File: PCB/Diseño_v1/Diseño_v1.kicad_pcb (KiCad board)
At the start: 2 copper layers, 100 x 100 mm, 7 parts

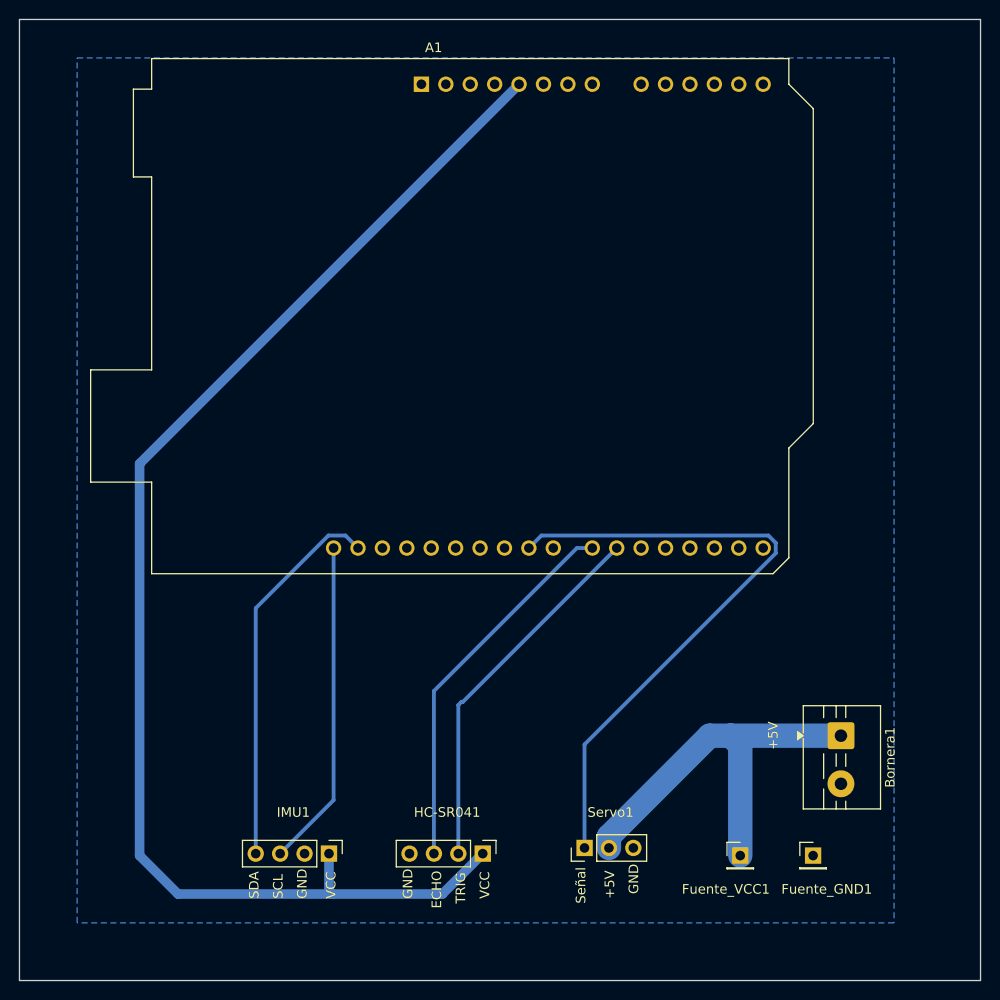
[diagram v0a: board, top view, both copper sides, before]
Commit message: Modifiqué el PCB
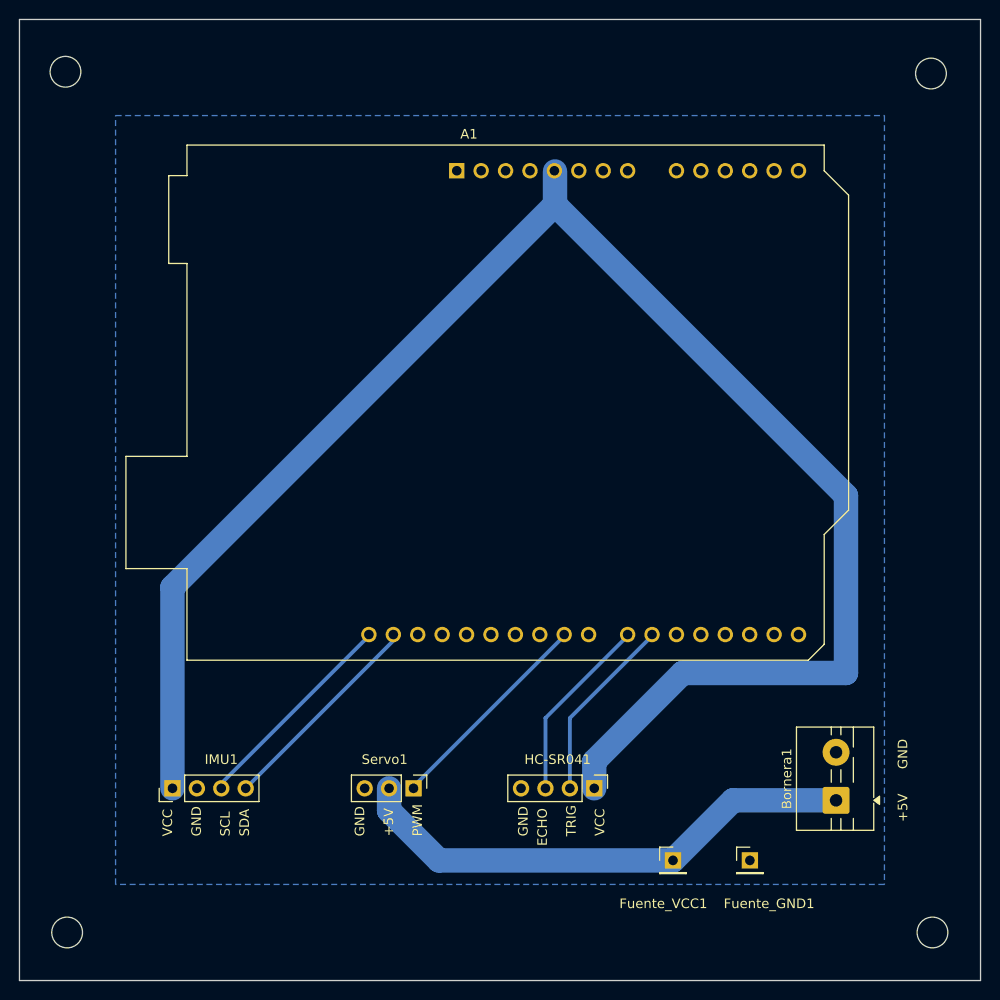
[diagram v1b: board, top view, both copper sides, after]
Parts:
- added REF**: MountingHole_3.2mm_M3, MountingHole:MountingHole_3.2mm_M3, F.Cu at (105.0, 145.0)
- added REF**: MountingHole_3.2mm_M3, MountingHole:MountingHole_3.2mm_M3, F.Cu at (195.0, 145.0)
- added REF**: MountingHole_3.2mm_M3, MountingHole:MountingHole_3.2mm_M3, F.Cu at (104.8, 55.4)
- added REF**: MountingHole_3.2mm_M3, MountingHole:MountingHole_3.2mm_M3, F.Cu at (194.8, 55.6)
- moved Servo1 18.8 mm to (141.0, 130.0), turned to -90 degrees
- moved IMU1 17.6 mm to (115.9, 130.0), turned to 90 degrees
- moved HC-SR041 13.4 mm to (159.8, 130.0)
- moved A1 9.72 mm to (145.5, 65.7)
- moved Fuente_VCC1 7.02 mm to (168.0, 137.5)
- moved Bornera1 6.74 mm to (185.0, 131.2), turned to 90 degrees
- moved Fuente_GND1 6.60 mm to (176.0, 137.5)
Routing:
- net /Señal: track 66.5 -> 22.4 mm
- net VCC: track 140.0 -> 174.7 mm
- net /Echo: track 39.6 -> 19.5 mm
- net /Trig: track 38.7 -> 19.5 mm
- net /SDA: track 39.9 -> 22.3 mm
- net /SCL: track 34.1 -> 22.3 mm
- net Net-(Bornera1-Pin_1): track 42.6 -> 53.6 mm
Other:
- board text added: "PWM"
- board text removed: "Señal"

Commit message: Volví a cambiar el PCB
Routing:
- net /Señal: track 22.4 -> 25.2 mm
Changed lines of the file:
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@@
 	)
 	(segment
-		(start 141 130)
-		(end 141 129.82)
-		(width 0.4)
+		(start 146.679161 124)
+		(end 142 124)
+		(width 0.6)
 		(layer "B.Cu")
 		(net "/Señal")
 	)
 	(segment
-		(start 141 129.82)
-		(end 156.745 114.075)
-		(width 0.4)
+		(start 141 125)
+		(end 141 130)
+		(width 0.6)
+		(layer "B.Cu")
+		(net "/Señal")
+	)
+	(segment
+		(start 142 124)
+		(end 141 125)
+		(width 0.6)
+		(layer "B.Cu")
+		(net "/Señal")
+	)
+	(segment
+		(start 156.679802 113.999359)
+		(end 146.679161 124)
+		(width 0.6)
 		(layer "B.Cu")
 		(net "/Señal")
@@
 	)
 	(segment
-		(start 165.885 114.075)
-		(end 157.27 122.69)
-		(width 0.4)
+		(start 157.27 122.549161)
+		(end 157.27 130)
+		(width 0.6)
 		(layer "B.Cu")
 		(net "/Trig")
 	)
 	(segment
-		(start 157.27 122.69)
-		(end 157.27 130)
-		(width 0.4)
+		(start 165.819802 113.999359)
+		(end 157.27 122.549161)
+		(width 0.6)
 		(layer "B.Cu")
 		(net "/Trig")
 	)
 	(segment
-		(start 154.73 130)
-		(end 154.73 122.69)
-		(width 0.4)
+		(start 154.73 122.549161)
+		(end 154.73 130)
+		(width 0.6)
 		(layer "B.Cu")
 		(net "/Echo")
 	)
 	(segment
-		(start 154.73 122.69)
-		(end 163.345 114.075)
-		(width 0.4)
+		(start 163.279802 113.999359)
+		(end 154.73 122.549161)
+		(width 0.6)
 		(layer "B.Cu")
 		(net "/Echo")
 	)
 	(segment
-		(start 123.54 130)
-		(end 138.965 114.575)
-		(width 0.4)
+		(start 138.899802 114.640198)
+		(end 138.899802 113.999359)
+		(width 0.6)
 		(layer "B.Cu")
 		(net "/SDA")
 	)
 	(segment
-		(start 138.965 114.575)
-		(end 138.965 114.075)
-		(width 0.4)
+		(start 123.54 130)
+		(end 138.899802 114.640198)
+		(width 0.6)
 		(layer "B.Cu")
 		(net "/SDA")
 	)
 	(segment
-		(start 136.425 114.075)
-		(end 121 129.5)
-		(width 0.4)
+		(start 121 129.359161)
+		(end 121 130)
+		(width 0.6)
 		(layer "B.Cu")
 		(net "/SCL")
 	)
 	(segment
-		(start 121 129.5)
-		(end 121 130)
-		(width 0.4)
+		(start 136.359802 113.999359)
+		(end 121 129.359161)
+		(width 0.6)
 		(layer "B.Cu")
 		(net "/SCL")
